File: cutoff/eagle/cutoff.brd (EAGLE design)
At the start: 40 x 45 mm, 29 parts, among them K1 RELAY, U1 LM2931ADT-5.0RKG, U2 NUD3160, U3 ATMEGA328, Y1 16MHz

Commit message: Ready for final routing.
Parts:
- added C8: 0.1uF, resistor:C0603K
- added D4: MBR0540, cutoff:SOD123FL
- moved R6 15.5 mm to (16.8, 12.5)
- moved R5 5.46 mm to (33.6, 20.8)
- moved C6 1.17 mm to (22.7, 4.70)
- moved C7 1.02 mm to (27.1, 19.0), turned to 90 degrees
- moved K1 1.00 mm to (23.2, 35.6)
- moved C5 0.92 mm to (14.5, 18.4)
- moved Y1 0.80 mm to (26.7, 3.32)
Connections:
- removed net CONTROL: U2.1, U3.22
- new net AREF: C8.1, U3.20
- new net RELAY: U2.1, U3.24
- net +12V: now also D4.C
- net GND: now also C8.2
- net N$1: now also D4.A
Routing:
- net RELAY: track 0.00 -> 12.4 mm, vias 0 -> 2
- net VSENSE: track 2.54 -> 14.1 mm, vias 0 -> 2
- net N$1: track 14.5 -> 25.1 mm
- net +5V: track 40.0 -> 49.1 mm
- net RXI: track 0.00 -> 3.25 mm
- net TXO: track 0.00 -> 3.25 mm
- net S-5V: track 0.00 -> 3.25 mm
- net RESET: track 0.00 -> 3.23 mm
- net DTR: track 0.00 -> 3.00 mm
- net AREF: track 0.00 -> 2.12 mm
- net +12V: track 29.3 -> 31.0 mm
- net N$4: track 15.5 -> 14.5 mm
- net N$5: track 22.3 -> 21.3 mm
- net GND: track 174.1 -> 174.8 mm, vias 14 -> 15
- net VBAT: track 28.7 -> 29.4 mm
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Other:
- outline, holes or cut-outs redrawn

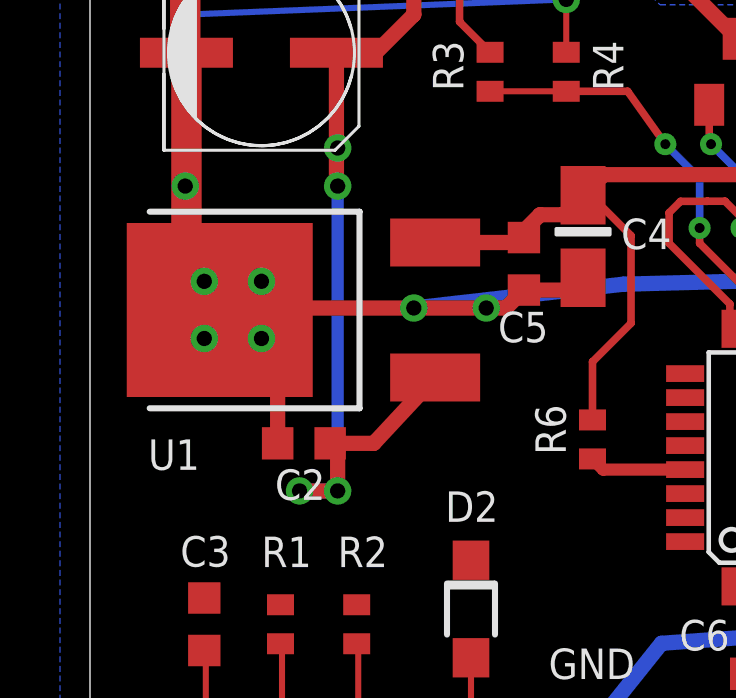
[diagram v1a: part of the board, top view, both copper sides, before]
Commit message: Moved cap away from LDO
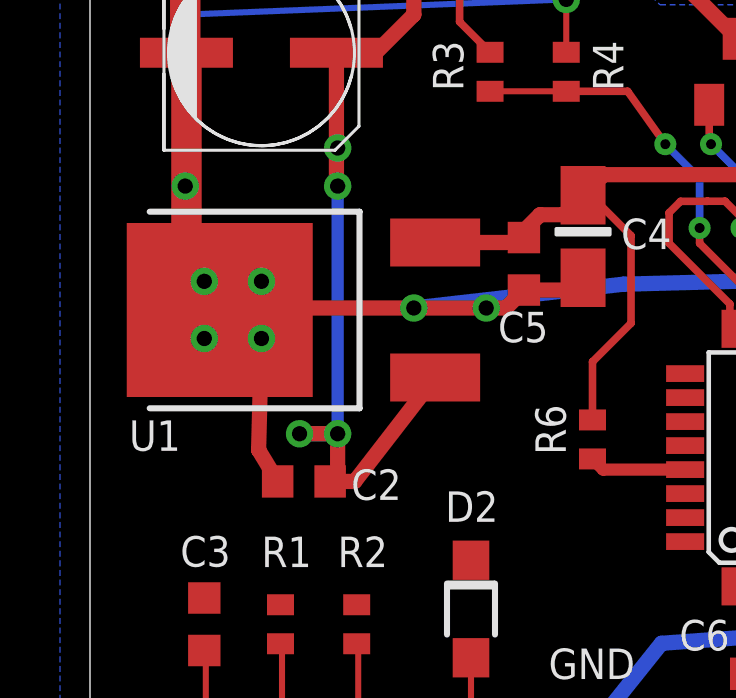
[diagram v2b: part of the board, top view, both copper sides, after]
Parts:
- moved C2 1.27 mm to (7.13, 11.1)
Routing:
- net GND: track 174.8 -> 176.1 mm
- net N$6: track 28.6 -> 27.5 mm
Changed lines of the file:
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@@
 <attribute name="VALUE" x="12.814" y="19.164" size="1.016" layer="27" rot="R270"/>
 </element>
-<element name="C2" library="resistor" package="C0603K" value="0.1uF" x="7.13" y="12.38" smashed="yes" rot="R180">
-<attribute name="NAME" x="6.167" y="10.495" size="1.016" layer="25" font="vector" ratio="10"/>
-<attribute name="VALUE" x="7.93" y="14.03" size="1.016" layer="27" rot="R180"/>
+<element name="C2" library="resistor" package="C0603K" value="0.1uF" x="7.13" y="11.11" smashed="yes" rot="R180">
+<attribute name="NAME" x="8.707" y="10.495" size="1.016" layer="25" font="vector" ratio="10"/>
+<attribute name="VALUE" x="7.93" y="12.76" size="1.016" layer="27" rot="R180"/>
 </element>
 <element name="C6" library="resistor" package="C0603K" value="0.1uF" x="22.733" y="4.699" smashed="yes" rot="R180">
@@
 </element>
 <element name="U1" library="cutoff" package="LDO" value="LM2931ADT-5.0RKG" x="6.825" y="16.825" smashed="yes" rot="R90">
-<attribute name="NAME" x="1.938" y="11.496" size="1.016" layer="25" font="vector" ratio="10"/>
+<attribute name="NAME" x="1.303" y="12.131" size="1.016" layer="25" font="vector" ratio="10"/>
 <attribute name="VALUE" x="9.365" y="21.905" size="1.27" layer="27" rot="R180"/>
 </element>
@@
 <wire x1="4.765" y1="16.825" x2="5.715" y2="15.875" width="0.508" layer="1"/>
 <via x="3.175" y="20.955" extent="1-16" drill="0.508"/>
-<wire x1="6.255" y1="12.38" x2="6.255" y2="15.335" width="0.508" layer="1"/>
-<wire x1="6.255" y1="15.335" x2="5.715" y2="15.875" width="0.508" layer="1"/>
+<wire x1="6.255" y1="11.11" x2="5.62" y2="12.16" width="0.508" layer="1"/>
+<wire x1="5.62" y1="12.16" x2="5.715" y2="15.875" width="0.508" layer="1"/>
 <wire x1="4.826" y1="16.891" x2="4.445" y2="16.51" width="0.508" layer="1"/>
 <wire x1="10.795" y1="16.891" x2="5.08" y2="16.891" width="0.508" layer="1"/>
@@
 <contactref element="C2" pad="1"/>
 <via x="8.255" y="20.955" extent="1-16" drill="0.508"/>
-<wire x1="8.255" y1="20.955" x2="8.255" y2="10.795" width="0.4064" layer="16"/>
-<via x="8.255" y="10.795" extent="1-16" drill="0.508"/>
+<wire x1="8.255" y1="20.955" x2="8.255" y2="12.7" width="0.4064" layer="16"/>
+<via x="8.255" y="12.7" extent="1-16" drill="0.508"/>
 <wire x1="10.795" y1="28.855" x2="10.795" y2="26.67" width="0.508" layer="1"/>
 <wire x1="10.795" y1="26.67" x2="9.525" y2="25.4" width="0.508" layer="1"/>
@@
 <wire x1="8.215" y1="20.995" x2="8.255" y2="20.955" width="0.508" layer="1"/>
 <via x="8.255" y="22.225" extent="1-16" drill="0.508"/>
-<wire x1="8.255" y1="10.795" x2="8.255" y2="12.13" width="0.508" layer="1"/>
-<wire x1="8.255" y1="12.13" x2="8.005" y2="12.38" width="0.508" layer="1"/>
-<via x="6.985" y="10.795" extent="1-16" drill="0.508"/>
-<wire x1="6.985" y1="10.795" x2="8.255" y2="10.795" width="0.508" layer="1"/>
-<wire x1="6.985" y1="10.795" x2="8.255" y2="10.795" width="0.508" layer="16"/>
-<wire x1="8.005" y1="12.38" x2="9.46" y2="12.38" width="0.508" layer="1"/>
-<wire x1="9.46" y1="12.38" x2="11.505" y2="14.575" width="0.508" layer="1"/>
+<wire x1="8.255" y1="12.7" x2="8.255" y2="11.495" width="0.508" layer="1"/>
+<wire x1="8.255" y1="11.495" x2="8.005" y2="11.11" width="0.508" layer="1"/>
+<via x="6.985" y="12.7" extent="1-16" drill="0.508"/>
+<wire x1="6.985" y1="12.7" x2="8.255" y2="12.7" width="0.508" layer="1"/>
+<wire x1="6.985" y1="12.7" x2="8.255" y2="12.7" width="0.508" layer="16"/>
+<wire x1="8.005" y1="11.11" x2="8.825" y2="11.11" width="0.508" layer="1"/>
+<wire x1="8.825" y1="11.11" x2="11.505" y2="14.575" width="0.508" layer="1"/>
 <wire x1="8.2296" y1="22.2504" x2="8.255" y2="22.225" width="0.2032" layer="1"/>
 <wire x1="8.2296" y1="22.2504" x2="8.215" y2="22.2504" width="0.2032" layer="1"/>

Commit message: A few tweaks before final auto routing.
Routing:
- net +5V: track 49.1 -> 71.4 mm
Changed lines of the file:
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@@
 <rectangle x1="3.175" y1="0" x2="17.145" y2="1.905" layer="41"/>
 <rectangle x1="38.1" y1="2.54" x2="40.005" y2="9.525" layer="41"/>
-<rectangle x1="25.4" y1="1.27" x2="27.94" y2="1.905" layer="41"/>
+<rectangle x1="22.86" y1="1.27" x2="30.48" y2="1.905" layer="41"/>
 <rectangle x1="12.065" y1="7.112" x2="13.335" y2="7.62" layer="41"/>
 <rectangle x1="12.065" y1="5.715" x2="13.462" y2="6.35" layer="41"/>
@@
 <wire x1="17.121" y1="21.336" x2="27.813" y2="21.336" width="0.508" layer="1"/>
 <wire x1="27.813" y1="21.336" x2="28.575" y2="20.574" width="0.508" layer="1"/>
-<wire x1="28.575" y1="20.574" x2="28.575" y2="18.344" width="0.508" layer="1"/>
 <wire x1="25.33" y1="7.6124" x2="25.33" y2="9.144" width="0.508" layer="1"/>
 <wire x1="25.33" y1="9.144" x2="25.33" y2="12.33" width="0.508" layer="1"/>
@@
 <wire x1="37.4904" y1="8.7376" x2="37.545" y2="8.81" width="0.2032" layer="1"/>
 <wire x1="23.6728" y1="4.6736" x2="23.608" y2="4.699" width="0.2032" layer="1"/>
-<wire x1="28.575" y1="18.344" x2="28.321" y2="18.09" width="0.4064" layer="1"/>
-<wire x1="28.321" y1="18.09" x2="27.05" y2="18.09" width="0.4064" layer="1"/>
-<wire x1="16.75" y1="13.16" x2="16.75" y2="15.099" width="0.254" layer="1"/>
-<wire x1="16.75" y1="15.099" x2="18.034" y2="16.383" width="0.254" layer="1"/>
-<wire x1="18.034" y1="16.383" x2="18.034" y2="19.304" width="0.254" layer="1"/>
-<wire x1="18.034" y1="19.304" x2="17.018" y2="20.32" width="0.254" layer="1"/>
 <wire x1="17.018" y1="20.32" x2="16.51" y2="20.32" width="0.254" layer="1"/>
-<wire x1="26.13" y1="13.13" x2="37.4904" y2="8.7376" width="0" layer="19" extent="1-1"/>
-<wire x1="16.51" y1="20.32" x2="16.435" y2="20.65" width="0" layer="19" extent="1-1"/>
-<wire x1="12.7" y1="8.5344" x2="16.75" y2="13.16" width="0" layer="19" extent="1-1"/>
+<wire x1="37.4904" y1="8.7376" x2="37.4904" y2="12.0396" width="0.508" layer="1"/>
+<wire x1="37.4904" y1="12.0396" x2="31.44" y2="18.09" width="0.508" layer="1"/>
+<wire x1="31.44" y1="18.09" x2="28.575" y2="18.09" width="0.508" layer="1"/>
+<wire x1="28.575" y1="18.09" x2="27.05" y2="18.09" width="0.508" layer="1"/>
+<wire x1="28.575" y1="20.574" x2="28.575" y2="18.09" width="0.508" layer="1"/>
+<wire x1="17.018" y1="20.32" x2="18.161" y2="19.177" width="0.508" layer="1"/>
+<wire x1="18.161" y1="19.177" x2="18.161" y2="16.256" width="0.508" layer="1"/>
+<wire x1="18.161" y1="16.256" x2="16.75" y2="14.845" width="0.508" layer="1"/>
+<wire x1="16.75" y1="14.845" x2="16.75" y2="13.16" width="0.508" layer="1"/>
+<wire x1="16.435" y1="20.65" x2="16.51" y2="20.32" width="0" layer="19" extent="1-1"/>
+<wire x1="12.7" y1="8.5344" x2="13.97" y2="9.8044" width="0.508" layer="1"/>
+<wire x1="13.97" y1="9.8044" x2="13.97" y2="12.065" width="0.508" layer="1"/>
+<wire x1="13.97" y1="12.065" x2="15.065" y2="13.16" width="0.508" layer="1"/>
+<wire x1="15.065" y1="13.16" x2="16.75" y2="13.16" width="0.508" layer="1"/>
 </signal>
 <signal name="SER_RX">
@@
 <contactref element="JP3" pad="3"/>
 <contactref element="D2" pad="A"/>
-<wire x1="12.7" y1="3.7592" x2="12.7" y2="5.233" width="0.2032" layer="1"/>
-<wire x1="11.4808" y1="2.54" x2="12.7" y2="3.7592" width="0.2032" layer="1"/>
+<wire x1="12.7" y1="3.7592" x2="12.7" y2="5.233" width="0.508" layer="1"/>
+<wire x1="11.4808" y1="2.54" x2="12.7" y2="3.7592" width="0.508" layer="1"/>
 <wire x1="11.4808" y1="2.54" x2="11.43" y2="2.54" width="0.2032" layer="1"/>
 </signal>

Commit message: Performed final auto routing.
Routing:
- net RESET: track 3.23 -> 43.4 mm, vias 0 -> 2
- net MOSI: track 0.00 -> 17.1 mm
- net SER_TX: track 0.00 -> 15.9 mm, vias 0 -> 2
- net SCK: track 0.00 -> 13.4 mm, vias 0 -> 1
- net SER_RX: track 0.00 -> 12.5 mm
- net LED: track 0.00 -> 9.79 mm, vias 0 -> 2
- net MISO: track 0.00 -> 9.34 mm, vias 0 -> 1
- net N$3: track 0.00 -> 4.96 mm
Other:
- board text added: "12VDC BAT CUTOFF REV 1"
- board text removed: "BAT CUTOFF REV1"
